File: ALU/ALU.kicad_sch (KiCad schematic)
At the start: 6 parts, among them J1 Conn_01x11_Socket, J2 A Reg, J3 Output, J4 Control Header, J5 B Reg, J6 Conn_01x10_Socket

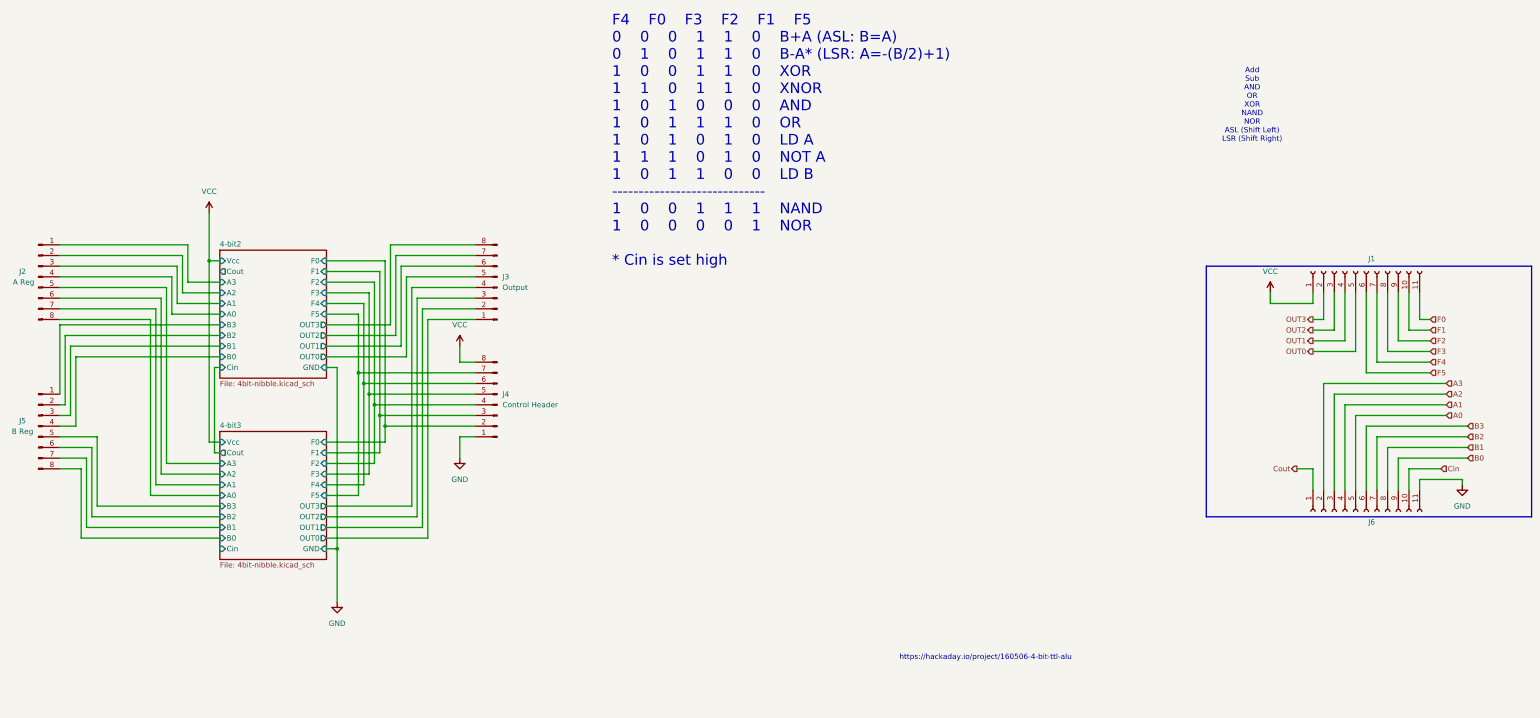
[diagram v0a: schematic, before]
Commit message: Create Flag/Status Register
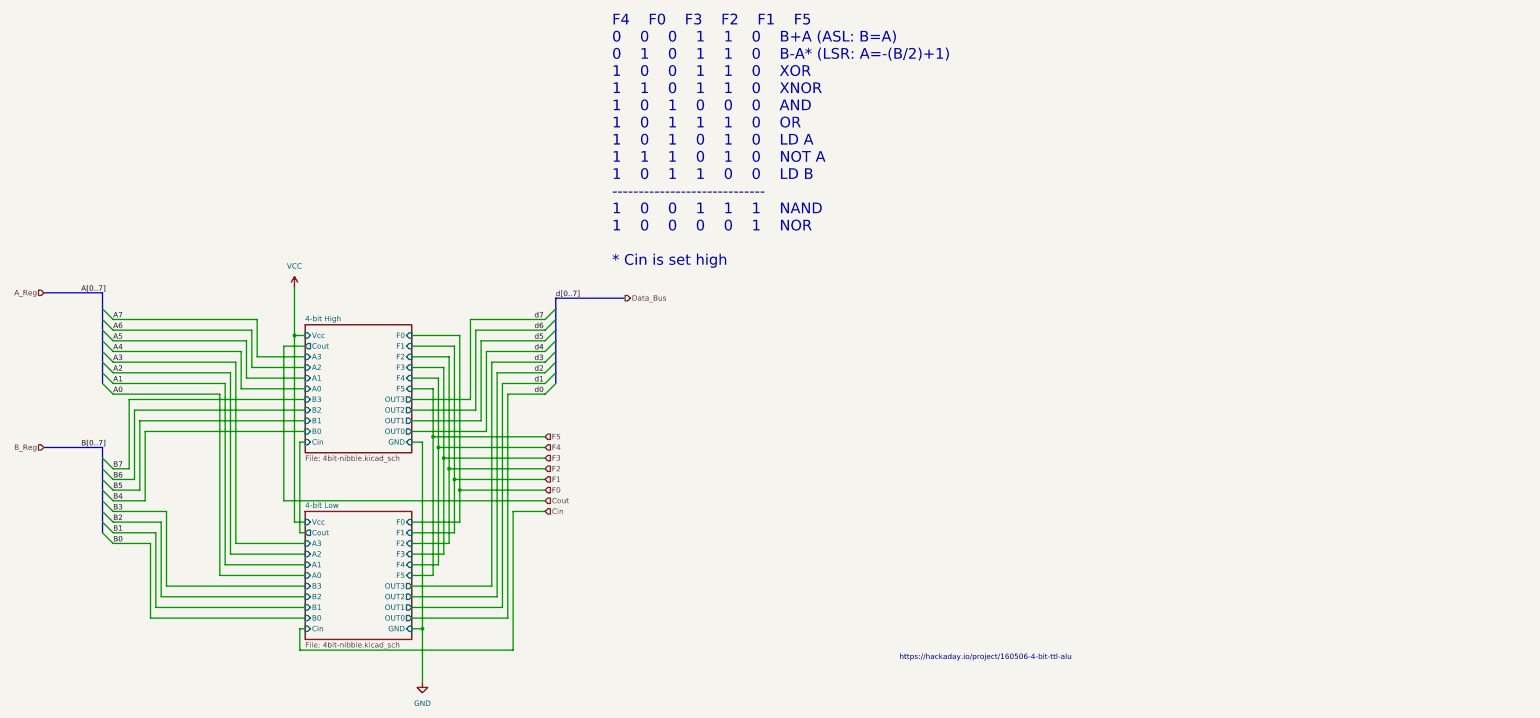
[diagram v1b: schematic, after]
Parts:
- removed J1: Conn_01x11_Socket, Connector_PinSocket_2.54mm:PinSocket_1x11_P2.54mm_Vertical, symbol Connector:Conn_01x11_Socket
- removed J2: A Reg, Connector_PinHeader_2.54mm:PinHeader_1x08_P2.54mm_Vertical, symbol Connector:Conn_01x08_Pin
- removed J3: Output, Connector_PinHeader_2.54mm:PinHeader_1x08_P2.54mm_Vertical, symbol Connector:Conn_01x08_Pin
- removed J4: Control Header, Connector_PinSocket_2.54mm:PinSocket_1x08_P2.54mm_Vertical, symbol Connector:Conn_01x08_Pin
- removed J5: B Reg, Connector_PinHeader_2.54mm:PinHeader_1x08_P2.54mm_Vertical, symbol Connector:Conn_01x08_Pin
- removed J6: Conn_01x10_Socket, Connector_PinSocket_2.54mm:PinSocket_1x11_P2.54mm_Vertical, symbol Connector:Conn_01x11_Socket
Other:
- sheet 4-bit2 renamed 4-bit High
- sheet 4-bit3 renamed 4-bit Low
- note removed: "Add Sub AND OR XOR NAND NOR ASL (Shift Left) LSR (Shift Right)"
